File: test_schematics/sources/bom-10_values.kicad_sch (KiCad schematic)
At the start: 10 parts, among them Q1 NMOS, Q2 NMOS_GSD

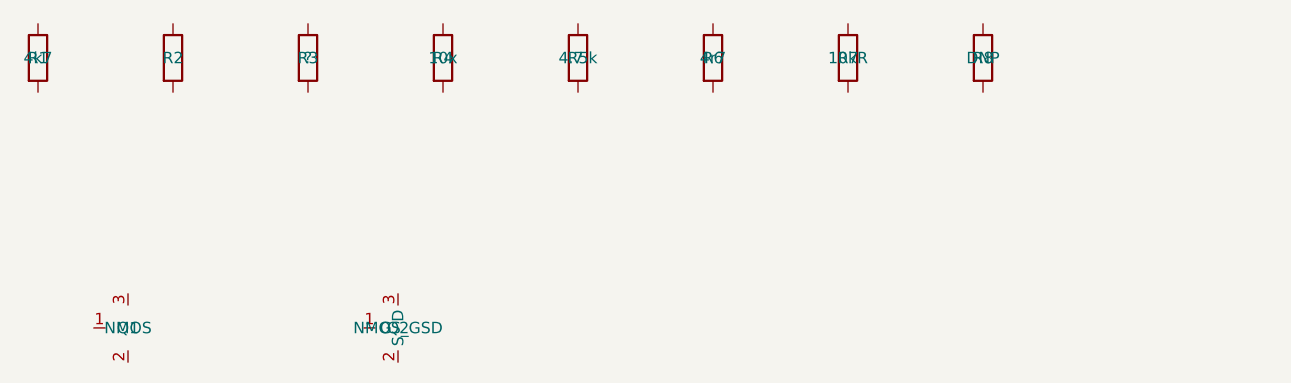
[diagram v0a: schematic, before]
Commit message: erc_analysis: part classes, values, graph queries and the I2C bus recogniser ported from erc_core; test schematics renamed <id>_<slug>, LIB-3 split out of the values schematic
Co-Authored-By: Claude Opus 5.5 <noreply@anthropic.com>
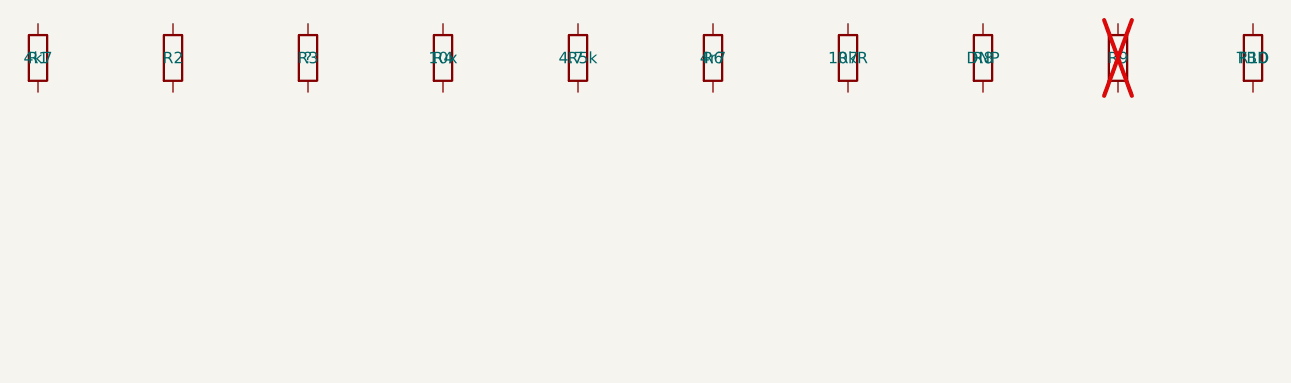
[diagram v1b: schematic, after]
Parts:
- removed Q1: NMOS, symbol Fixture:NMOS
- removed Q2: NMOS_GSD, symbol Fixture:NMOS_GSD
- added R10: TBD, symbol Fixture:R
- added R9: ?, symbol Fixture:R
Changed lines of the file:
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@@
 		(instances (project "test_schematics" (path "/5717e000-0000-4000-8000-000000000000" (reference "R8") (unit 1))))
 	)
-	(symbol (lib_id "Fixture:NMOS") (at 40 80 0) (unit 1) (exclude_from_sim no) (in_bom yes) (on_board yes) (dnp no)
-		(property "Reference" "Q1" (at 40 80 0) (effects (font (size 1.27 1.27))))
-		(property "Value" "NMOS" (at 40 80 0) (effects (font (size 1.27 1.27))))
-		(property "Footprint" "" (at 40 80 0) (effects (font (size 1.27 1.27)) (hide yes)))
-		(property "Datasheet" "" (at 40 80 0) (effects (font (size 1.27 1.27)) (hide yes)))
-		(property "Description" "N-Channel MOSFET" (at 40 80 0) (effects (font (size 1.27 1.27)) (hide yes)))
+	(symbol (lib_id "Fixture:R") (at 150 50 0) (unit 1) (exclude_from_sim no) (in_bom yes) (on_board yes) (dnp yes)
+		(property "Reference" "R9" (at 150 50 0) (effects (font (size 1.27 1.27))))
+		(property "Value" "?" (at 150 50 0) (effects (font (size 1.27 1.27))))
+		(property "Footprint" "" (at 150 50 0) (effects (font (size 1.27 1.27)) (hide yes)))
+		(property "Datasheet" "" (at 150 50 0) (effects (font (size 1.27 1.27)) (hide yes)))
+		(property "Description" "Resistor" (at 150 50 0) (effects (font (size 1.27 1.27)) (hide yes)))
 		(pin "1")
 		(pin "2")
-		(pin "3")
-		(instances (project "test_schematics" (path "/5717e000-0000-4000-8000-000000000000" (reference "Q1") (unit 1))))
+		(instances (project "test_schematics" (path "/5717e000-0000-4000-8000-000000000000" (reference "R9") (unit 1))))
 	)
-	(symbol (lib_id "Fixture:NMOS_GSD") (at 70 80 0) (unit 1) (exclude_from_sim no) (in_bom yes) (on_board yes) (dnp no)
-		(property "Reference" "Q2" (at 70 80 0) (effects (font (size 1.27 1.27))))
-		(property "Value" "NMOS_GSD" (at 70 80 0) (effects (font (size 1.27 1.27))))
-		(property "Footprint" "" (at 70 80 0) (effects (font (size 1.27 1.27)) (hide yes)))
-		(property "Datasheet" "" (at 70 80 0) (effects (font (size 1.27 1.27)) (hide yes)))
-		(property "Description" "N-Channel MOSFET" (at 70 80 0) (effects (font (size 1.27 1.27)) (hide yes)))
+	(symbol (lib_id "Fixture:R") (at 165 50 0) (unit 1) (exclude_from_sim no) (in_bom yes) (on_board yes) (dnp no)
+		(property "Reference" "R10" (at 165 50 0) (effects (font (size 1.27 1.27))))
+		(property "Value" "TBD" (at 165 50 0) (effects (font (size 1.27 1.27))))
+		(property "Footprint" "" (at 165 50 0) (effects (font (size 1.27 1.27)) (hide yes)))
+		(property "Datasheet" "" (at 165 50 0) (effects (font (size 1.27 1.27)) (hide yes)))
+		(property "Description" "Resistor" (at 165 50 0) (effects (font (size 1.27 1.27)) (hide yes)))
 		(pin "1")
 		(pin "2")
-		(pin "3")
-		(instances (project "test_schematics" (path "/5717e000-0000-4000-8000-000000000000" (reference "Q2") (unit 1))))
+		(instances (project "test_schematics" (path "/5717e000-0000-4000-8000-000000000000" (reference "R10") (unit 1))))
 	)
 	(sheet_instances (path "/" (page "1")))

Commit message: BOM-10: capacitors and inductors, the E-series test with the nearest E24/E96 values, the unit apart; bom-10_values grows R11..R13, C1..C3, L1, L2; availability tests for the new needs
Co-Authored-By: Claude Opus 5.5 <noreply@anthropic.com>
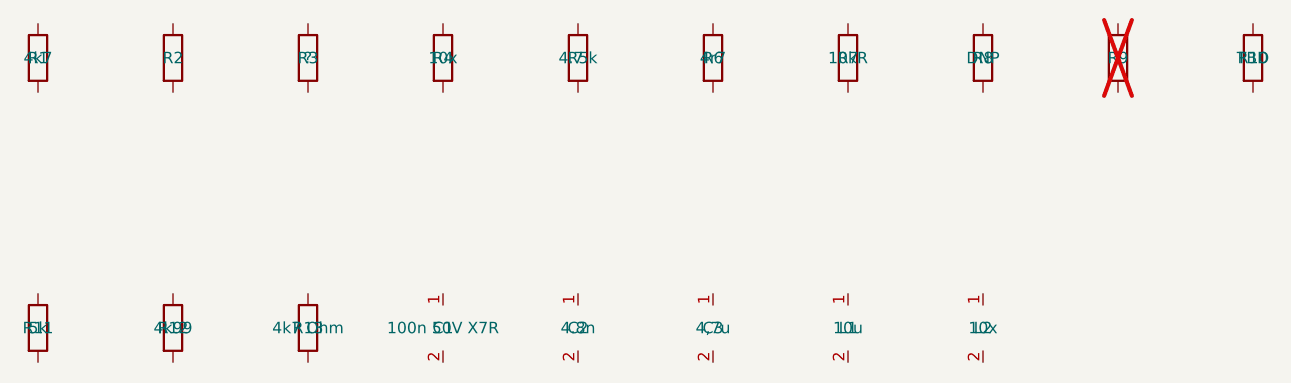
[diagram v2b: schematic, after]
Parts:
- added C1: 100n 50V X7R, symbol Fixture:C
- added C2: 4.8n, symbol Fixture:C
- added C3: 4,7u, symbol Fixture:C
- added L1: 10u, symbol Fixture:L
- added L2: 10x, symbol Fixture:L
- added R11: 5k, symbol Fixture:R
- added R12: 4k99, symbol Fixture:R
- added R13: 4k7 Ohm, symbol Fixture:R
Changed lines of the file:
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@@
 		(instances (project "test_schematics" (path "/5717e000-0000-4000-8000-000000000000" (reference "R10") (unit 1))))
 	)
+	(symbol (lib_id "Fixture:R") (at 30 80 0) (unit 1) (exclude_from_sim no) (in_bom yes) (on_board yes) (dnp no)
+		(property "Reference" "R11" (at 30 80 0) (effects (font (size 1.27 1.27))))
+		(property "Value" "5k" (at 30 80 0) (effects (font (size 1.27 1.27))))
+		(property "Footprint" "" (at 30 80 0) (effects (font (size 1.27 1.27)) (hide yes)))
+		(property "Datasheet" "" (at 30 80 0) (effects (font (size 1.27 1.27)) (hide yes)))
+		(pin "1")
+		(pin "2")
+		(instances (project "test_schematics" (path "/5717e000-0000-4000-8000-000000000000" (reference "R11") (unit 1)))))
+	(symbol (lib_id "Fixture:R") (at 45 80 0) (unit 1) (exclude_from_sim no) (in_bom yes) (on_board yes) (dnp no)
+		(property "Reference" "R12" (at 45 80 0) (effects (font (size 1.27 1.27))))
+		(property "Value" "4k99" (at 45 80 0) (effects (font (size 1.27 1.27))))
+		(property "Footprint" "" (at 45 80 0) (effects (font (size 1.27 1.27)) (hide yes)))
+		(property "Datasheet" "" (at 45 80 0) (effects (font (size 1.27 1.27)) (hide yes)))
+		(pin "1")
+		(pin "2")
+		(instances (project "test_schematics" (path "/5717e000-0000-4000-8000-000000000000" (reference "R12") (unit 1)))))
+	(symbol (lib_id "Fixture:R") (at 60 80 0) (unit 1) (exclude_from_sim no) (in_bom yes) (on_board yes) (dnp no)
+		(property "Reference" "R13" (at 60 80 0) (effects (font (size 1.27 1.27))))
+		(property "Value" "4k7 Ohm" (at 60 80 0) (effects (font (size 1.27 1.27))))
+		(property "Footprint" "" (at 60 80 0) (effects (font (size 1.27 1.27)) (hide yes)))
+		(property "Datasheet" "" (at 60 80 0) (effects (font (size 1.27 1.27)) (hide yes)))
+		(pin "1")
+		(pin "2")
+		(instances (project "test_schematics" (path "/5717e000-0000-4000-8000-000000000000" (reference "R13") (unit 1)))))
+	(symbol (lib_id "Fixture:C") (at 75 80 0) (unit 1) (exclude_from_sim no) (in_bom yes) (on_board yes) (dnp no)
+		(property "Reference" "C1" (at 75 80 0) (effects (font (size 1.27 1.27))))
+		(property "Value" "100n 50V X7R" (at 75 80 0) (effects (font (size 1.27 1.27))))
+		(property "Footprint" "" (at 75 80 0) (effects (font (size 1.27 1.27)) (hide yes)))
+		(property "Datasheet" "" (at 75 80 0) (effects (font (size 1.27 1.27)) (hide yes)))
+		(pin "1")
+		(pin "2")
+		(instances (project "test_schematics" (path "/5717e000-0000-4000-8000-000000000000" (reference "C1") (unit 1)))))
+	(symbol (lib_id "Fixture:C") (at 90 80 0) (unit 1) (exclude_from_sim no) (in_bom yes) (on_board yes) (dnp no)
+		(property "Reference" "C2" (at 90 80 0) (effects (font (size 1.27 1.27))))
+		(property "Value" "4.8n" (at 90 80 0) (effects (font (size 1.27 1.27))))
+		(property "Footprint" "" (at 90 80 0) (effects (font (size 1.27 1.27)) (hide yes)))
+		(property "Datasheet" "" (at 90 80 0) (effects (font (size 1.27 1.27)) (hide yes)))
+		(pin "1")
+		(pin "2")
+		(instances (project "test_schematics" (path "/5717e000-0000-4000-8000-000000000000" (reference "C2") (unit 1)))))
+	(symbol (lib_id "Fixture:C") (at 105 80 0) (unit 1) (exclude_from_sim no) (in_bom yes) (on_board yes) (dnp no)
+		(property "Reference" "C3" (at 105 80 0) (effects (font (size 1.27 1.27))))
+		(property "Value" "4,7u" (at 105 80 0) (effects (font (size 1.27 1.27))))
+		(property "Footprint" "" (at 105 80 0) (effects (font (size 1.27 1.27)) (hide yes)))
+		(property "Datasheet" "" (at 105 80 0) (effects (font (size 1.27 1.27)) (hide yes)))
+		(pin "1")
+		(pin "2")
+		(instances (project "test_schematics" (path "/5717e000-0000-4000-8000-000000000000" (reference "C3") (unit 1)))))
+	(symbol (lib_id "Fixture:L") (at 120 80 0) (unit 1) (exclude_from_sim no) (in_bom yes) (on_board yes) (dnp no)
+		(property "Reference" "L1" (at 120 80 0) (effects (font (size 1.27 1.27))))
+		(property "Value" "10u" (at 120 80 0) (effects (font (size 1.27 1.27))))
+		(property "Footprint" "" (at 120 80 0) (effects (font (size 1.27 1.27)) (hide yes)))
+		(property "Datasheet" "" (at 120 80 0) (effects (font (size 1.27 1.27)) (hide yes)))
+		(pin "1")
+		(pin "2")
+		(instances (project "test_schematics" (path "/5717e000-0000-4000-8000-000000000000" (reference "L1") (unit 1)))))
+	(symbol (lib_id "Fixture:L") (at 135 80 0) (unit 1) (exclude_from_sim no) (in_bom yes) (on_board yes) (dnp no)
+		(property "Reference" "L2" (at 135 80 0) (effects (font (size 1.27 1.27))))
+		(property "Value" "10x" (at 135 80 0) (effects (font (size 1.27 1.27))))
+		(property "Footprint" "" (at 135 80 0) (effects (font (size 1.27 1.27)) (hide yes)))
+		(property "Datasheet" "" (at 135 80 0) (effects (font (size 1.27 1.27)) (hide yes)))
+		(pin "1")
+		(pin "2")
+		(instances (project "test_schematics" (path "/5717e000-0000-4000-8000-000000000000" (reference "L2") (unit 1)))))
 	(sheet_instances (path "/" (page "1")))
 )
